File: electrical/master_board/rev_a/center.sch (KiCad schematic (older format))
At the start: 8 parts, among them CN50 HCSR04;F1X4, CN51 HCSR04LP;F1X4, CN52 HCSR04LP;F1X4, CN53 HCSR04LP;F1X4, CN54 HCSR04;F1X4, CN55 HR2_EncoderMate;2XF1X3, CN56 HR2_EncoderMate;2XF1X3, CN57 RASPI;F2X20

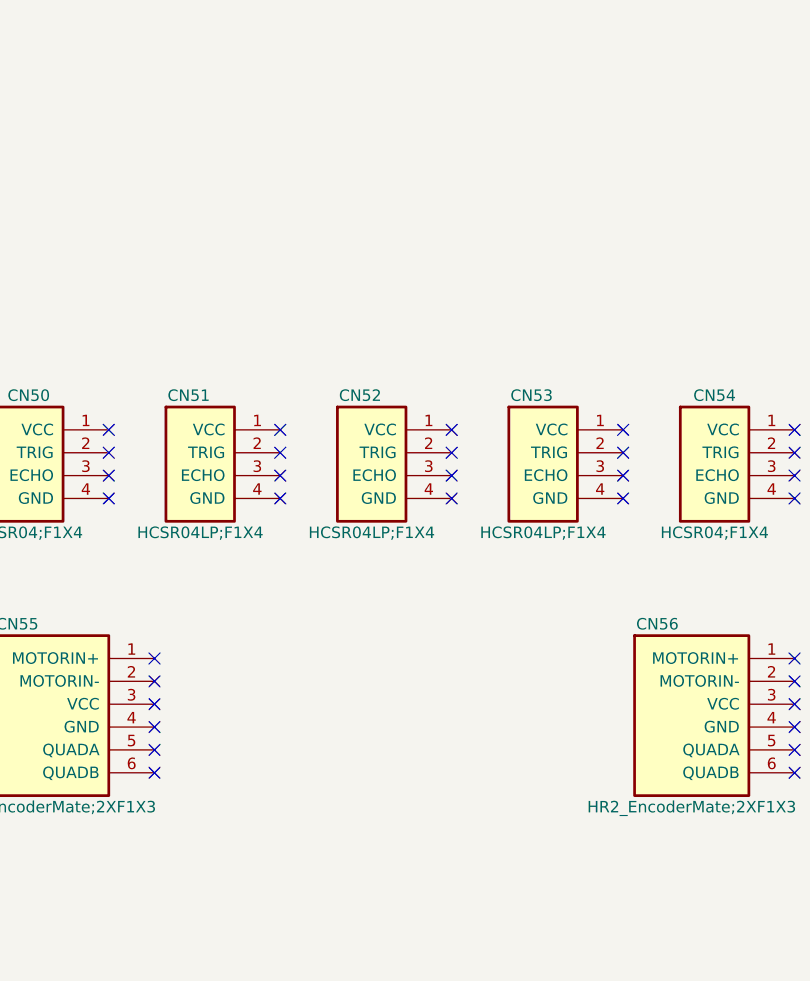
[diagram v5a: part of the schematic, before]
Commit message: Added .../st_adaptor/rev_a directory.  ST_MATE is properly integrated as a symbol/footprint.
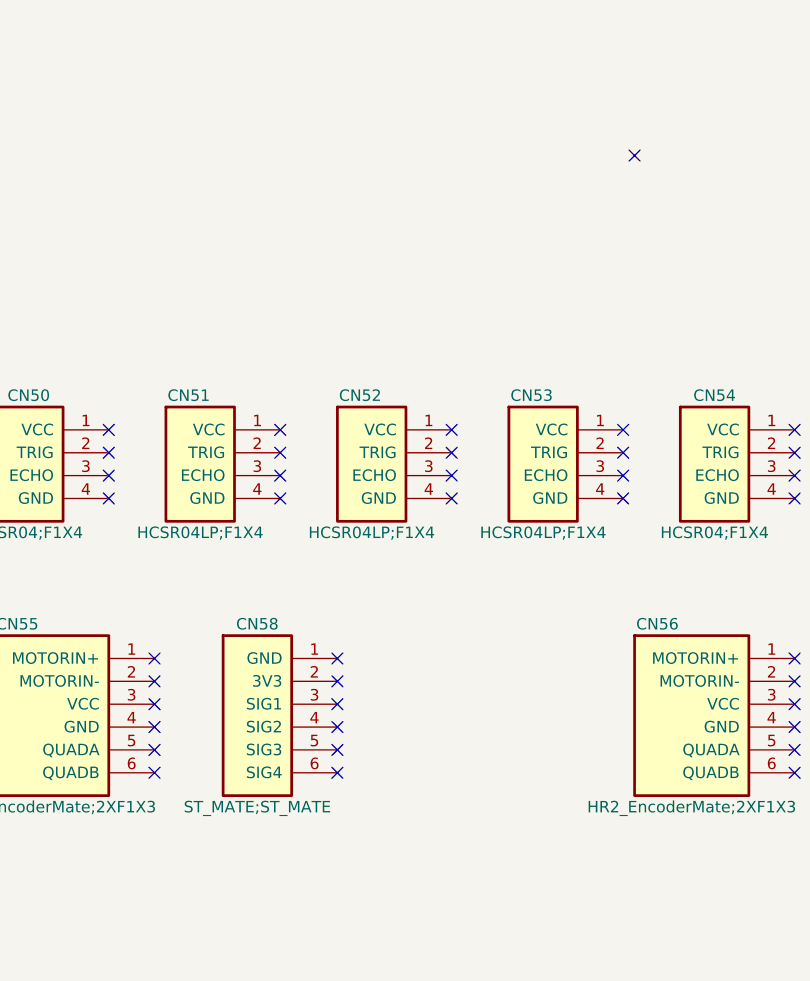
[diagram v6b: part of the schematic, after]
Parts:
- added CN58: ST_MATE;ST_MATE, HR2:ST_MATE, symbol HR2:ST_MATE;ST_MATE
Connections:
- no-connect marks 72 -> 79
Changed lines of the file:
@@
 	1    0    0    -1
 $EndComp
+$Comp
+L HR2:ST_MATE;ST_MATE CN58
+U 1 1 5F14D9D8
+P 3300 3600
+F 0 "CN58" H 3650 3750 50  0000 C CNN
+F 1 "ST_MATE;ST_MATE" H 3650 2950 50  0000 C CNN
+F 2 "HR2:ST_MATE" H 3500 3650 60  0001 L CNN
+F 3 "ST Adaptor Mating Connector" H 3500 3450 60  0001 L CNN
+	1    3300 3600
+	1    0    0    -1
+$EndComp
+NoConn ~ 4000 3600
+NoConn ~ 4000 3700
+NoConn ~ 4000 3800
+NoConn ~ 4000 3900
+NoConn ~ 4000 4000
+NoConn ~ 4000 4100
+NoConn ~ 5300 1400
 $EndSCHEMATC

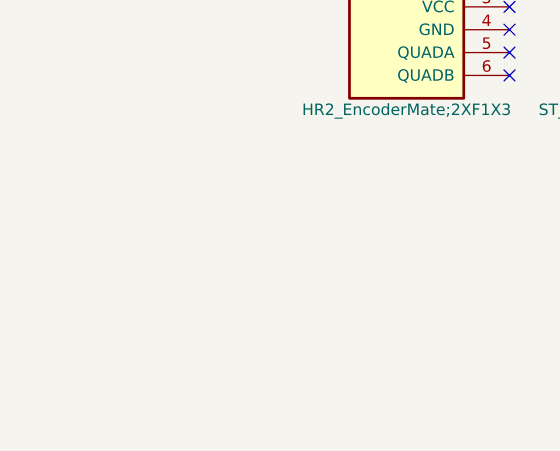
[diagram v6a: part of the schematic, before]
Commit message: Placed all of the Groves on the PCB's.
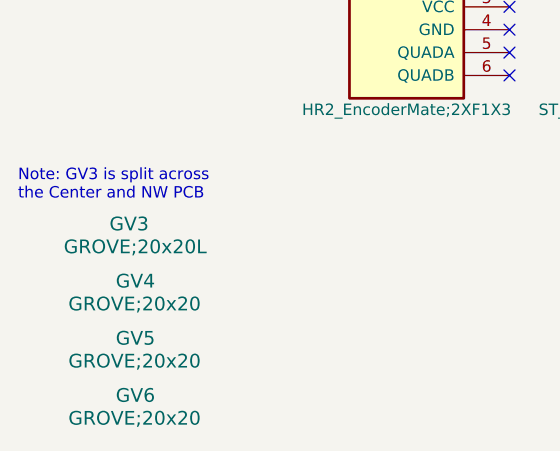
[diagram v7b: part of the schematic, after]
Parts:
- added GV3: GROVE;20x20L, HR2:GROVE20x20L, symbol HR2:GROVE;20x20L
- added GV4, GV5, GV6: GROVE;20x20, HR2:GROVE20x20, symbol HR2:GROVE;20x20
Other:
- note added: "Note: GV3 is split across\nthe Center and NW PCB"
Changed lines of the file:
@@
 NoConn ~ 4000 4100
 NoConn ~ 5300 1400
+$Comp
+L HR2:GROVE;20x20 GV4
+U 1 1 5F303EAE
+P 1600 5050
+F 0 "GV4" H 1550 5100 60  0000 L CNN
+F 1 "GROVE;20x20" H 1350 5000 60  0000 L CNN
+F 2 "HR2:GROVE20x20" H 1800 5100 60  0001 L CNN
+F 3 "Grove 20x20 Module" H 1800 4900 60  0001 L CNN
+F 4 "Grove 20x20 Module" H 1800 5000 60  0001 L CNN "manf#"
+	1    1600 5050
+	-1   0    0    -1
+$EndComp
+$Comp
+L HR2:GROVE;20x20 GV5
+U 1 1 5F304369
+P 1600 5300
+F 0 "GV5" H 1550 5350 60  0000 L CNN
+F 1 "GROVE;20x20" H 1350 5250 60  0000 L CNN
+F 2 "HR2:GROVE20x20" H 1800 5350 60  0001 L CNN
+F 3 "Grove 20x20 Module" H 1800 5150 60  0001 L CNN
+F 4 "Grove 20x20 Module" H 1800 5250 60  0001 L CNN "manf#"
+	1    1600 5300
+	-1   0    0    -1
+$EndComp
+$Comp
+L HR2:GROVE;20x20 GV6
+U 1 1 5F304374
+P 1600 5550
+F 0 "GV6" H 1550 5600 60  0000 L CNN
+F 1 "GROVE;20x20" H 1350 5500 60  0000 L CNN
+F 2 "HR2:GROVE20x20" H 1800 5600 60  0001 L CNN
+F 3 "Grove 20x20 Module" H 1800 5400 60  0001 L CNN
+F 4 "Grove 20x20 Module" H 1800 5500 60  0001 L CNN "manf#"
+	1    1600 5550
+	-1   0    0    -1
+$EndComp
+Text Notes 1050 4650 0    50   ~ 0
+Note: GV3 is split across\nthe Center and NW PCB
+$Comp
+L HR2:GROVE;20x20L GV3
+U 1 1 5F303927
+P 1550 4800
+F 0 "GV3" H 1450 4850 60  0000 L CNN
+F 1 "GROVE;20x20L" H 1250 4750 60  0000 L CNN
+F 2 "HR2:GROVE20x20L" H 1750 4850 60  0001 L CNN
+F 3 "Grove 20x20 Module" H 1750 4650 60  0001 L CNN
+F 4 "Grove 20x20 Module" H 1750 4750 60  0001 L CNN "manf#"
+	1    1550 4800
+	1    0    0    -1
+$EndComp
 $EndSCHEMATC

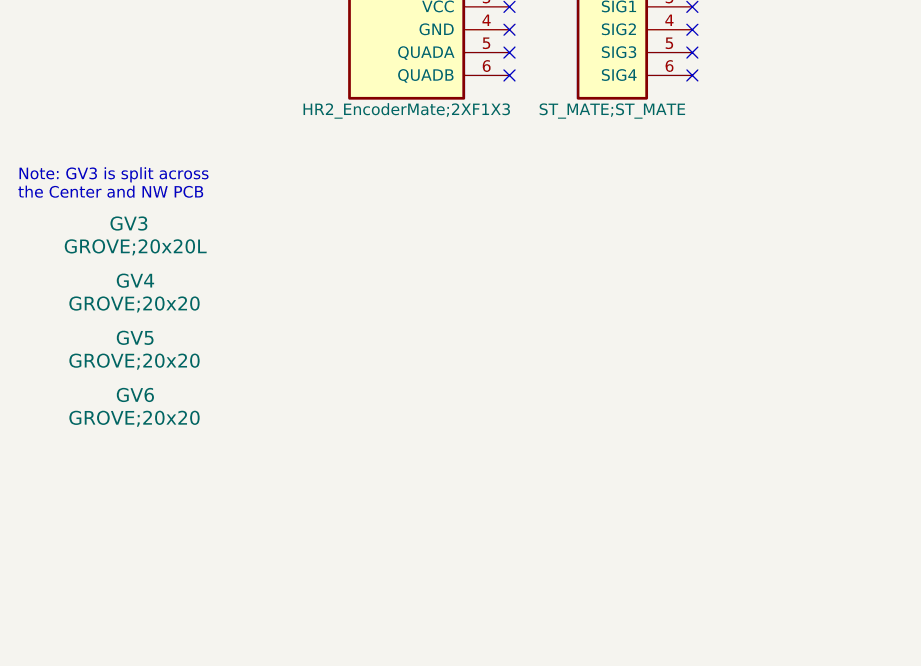
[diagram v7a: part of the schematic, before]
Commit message: Fixed Groves and added MikroBus's.
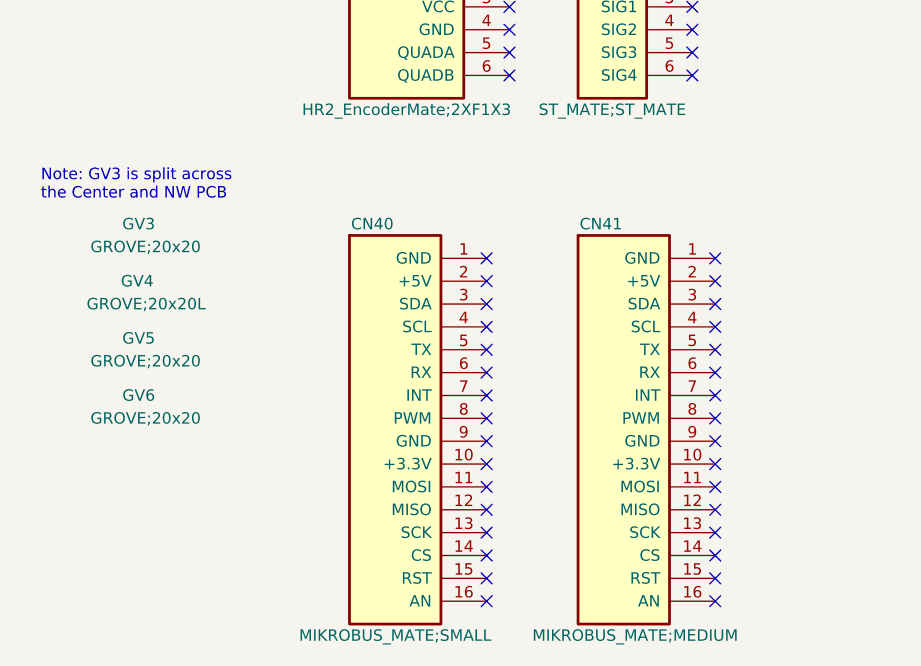
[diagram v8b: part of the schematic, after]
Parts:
- removed GV3: GROVE;20x20L, HR2:GROVE20x20L, symbol HR2:GROVE;20x20L
- removed GV4: GROVE;20x20, HR2:GROVE20x20, symbol HR2:GROVE;20x20
- added CN40: MIKROBUS_MATE;SMALL, HR2:MIKROBUS_SMALL_MATE, symbol HR2:MIKROBUS_MATE;SMALL
- added CN41: MIKROBUS_MATE;MEDIUM, HR2:MIKROBUS_MEDIUM_MATE, symbol HR2:MIKROBUS_MATE;MEDIUM
- added GV3: GROVE;20x20, HR2:GROVE20x20, symbol HR2:GROVE;20x20
- added GV4: GROVE;20x20L, HR2:GROVE20x20L, symbol HR2:GROVE;20x20L
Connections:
- no-connect marks 79 -> 111
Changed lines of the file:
@@
 NoConn ~ 5300 1400
-$Comp
-L HR2:GROVE;20x20 GV4
-U 1 1 5F303EAE
-P 1600 5050
-F 0 "GV4" H 1550 5100 60  0000 L CNN
-F 1 "GROVE;20x20" H 1350 5000 60  0000 L CNN
-F 2 "HR2:GROVE20x20" H 1800 5100 60  0001 L CNN
-F 3 "Grove 20x20 Module" H 1800 4900 60  0001 L CNN
-F 4 "Grove 20x20 Module" H 1800 5000 60  0001 L CNN "manf#"
-	1    1600 5050
-	-1   0    0    -1
-$EndComp
 $Comp
 L HR2:GROVE;20x20 GV5
 U 1 1 5F304369
 P 1600 5300
-F 0 "GV5" H 1550 5350 60  0000 L CNN
-F 1 "GROVE;20x20" H 1350 5250 60  0000 L CNN
+F 0 "GV5" H 1550 5350 50  0000 L CNN
+F 1 "GROVE;20x20" H 1350 5250 50  0000 L CNN
 F 2 "HR2:GROVE20x20" H 1800 5350 60  0001 L CNN
 F 3 "Grove 20x20 Module" H 1800 5150 60  0001 L CNN
@@
 U 1 1 5F304374
 P 1600 5550
-F 0 "GV6" H 1550 5600 60  0000 L CNN
-F 1 "GROVE;20x20" H 1350 5500 60  0000 L CNN
+F 0 "GV6" H 1550 5600 50  0000 L CNN
+F 1 "GROVE;20x20" H 1350 5500 50  0000 L CNN
 F 2 "HR2:GROVE20x20" H 1800 5600 60  0001 L CNN
 F 3 "Grove 20x20 Module" H 1800 5400 60  0001 L CNN
@@
 	-1   0    0    -1
 $EndComp
-Text Notes 1050 4650 0    50   ~ 0
+Text Notes 1150 4650 0    50   ~ 0
 Note: GV3 is split across\nthe Center and NW PCB
+NoConn ~ 3100 4900
+NoConn ~ 3100 5000
+NoConn ~ 3100 5100
+NoConn ~ 3100 5200
+NoConn ~ 3100 5300
+NoConn ~ 3100 5400
+NoConn ~ 3100 5500
+NoConn ~ 3100 5700
+NoConn ~ 3100 5600
+NoConn ~ 3100 5800
+NoConn ~ 4100 4900
+NoConn ~ 4100 5000
+NoConn ~ 4100 5100
+NoConn ~ 4100 5200
+NoConn ~ 4100 5300
+NoConn ~ 4100 5400
+NoConn ~ 4100 5500
+NoConn ~ 4100 5600
+NoConn ~ 4100 5700
+NoConn ~ 4100 5800
+NoConn ~ 4100 5900
+NoConn ~ 4100 6000
+NoConn ~ 4100 6100
+NoConn ~ 4100 6200
+NoConn ~ 4100 6300
+NoConn ~ 4100 6400
+NoConn ~ 3100 5900
+NoConn ~ 3100 6000
+NoConn ~ 3100 6100
+NoConn ~ 3100 6200
+NoConn ~ 3100 6300
+NoConn ~ 3100 6400
 $Comp
-L HR2:GROVE;20x20L GV3
-U 1 1 5F303927
-P 1550 4800
-F 0 "GV3" H 1450 4850 60  0000 L CNN
-F 1 "GROVE;20x20L" H 1250 4750 60  0000 L CNN
-F 2 "HR2:GROVE20x20L" H 1750 4850 60  0001 L CNN
-F 3 "Grove 20x20 Module" H 1750 4650 60  0001 L CNN
-F 4 "Grove 20x20 Module" H 1750 4750 60  0001 L CNN "manf#"
-	1    1550 4800
+L HR2:MIKROBUS_MATE;SMALL CN40
+U 1 1 5F305D69
+P 2300 4900
+F 0 "CN40" H 2600 5050 50  0000 C CNN
+F 1 "MIKROBUS_MATE;SMALL" H 2700 3250 50  0000 C CNN
+F 2 "HR2:MIKROBUS_SMALL_MATE" H 2500 4950 60  0001 L CNN
+F 3 "MikroBus Small Mate" H 2500 4750 60  0001 L CNN
+F 4 "MikroBus Small Mate" H 2500 4650 60  0001 L CNN "Field5"
+	1    2300 4900
 	1    0    0    -1
 $EndComp
+$Comp
+L HR2:MIKROBUS_MATE;MEDIUM CN41
+U 1 1 5F306A7C
+P 3300 4900
+F 0 "CN41" H 3600 5050 50  0000 C CNN
+F 1 "MIKROBUS_MATE;MEDIUM" H 3750 3250 50  0000 C CNN
+F 2 "HR2:MIKROBUS_MEDIUM_MATE" H 3500 4950 60  0001 L CNN
+F 3 "MikroBus Mate Medium" H 3500 4750 60  0001 L CNN
+F 4 "MikroBus Mate Medium" H 3500 4650 60  0001 L CNN "Field5"
+	1    3300 4900
+	1    0    0    -1
+$EndComp
+$Comp
+L HR2:GROVE;20x20L GV4
+U 1 1 5F30889D
+P 1600 5050
+F 0 "GV4" H 1500 5100 50  0000 L CNN
+F 1 "GROVE;20x20L" H 1350 5000 50  0000 L CNN
+F 2 "HR2:GROVE20x20L" H 1800 5100 60  0001 L CNN
+F 3 "Grove 20x20 Module" H 1800 4900 60  0001 L CNN
+F 4 "Grove 20x20 Module" H 1800 5000 60  0001 L CNN "manf#"
+	1    1600 5050
+	1    0    0    -1
+$EndComp
+$Comp
+L HR2:GROVE;20x20 GV3
+U 1 1 5F308FA7
+P 1600 4800
+F 0 "GV3" H 1550 4850 50  0000 L CNN
+F 1 "GROVE;20x20" H 1350 4750 50  0000 L CNN
+F 2 "HR2:GROVE20x20" H 1800 4850 60  0001 L CNN
+F 3 "Grove 20x20 Module" H 1800 4650 60  0001 L CNN
+F 4 "Grove 20x20 Module" H 1800 4750 60  0001 L CNN "manf#"
+	1    1600 4800
+	-1   0    0    -1
+$EndComp
 $EndSCHEMATC
